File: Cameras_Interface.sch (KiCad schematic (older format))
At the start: 18 parts

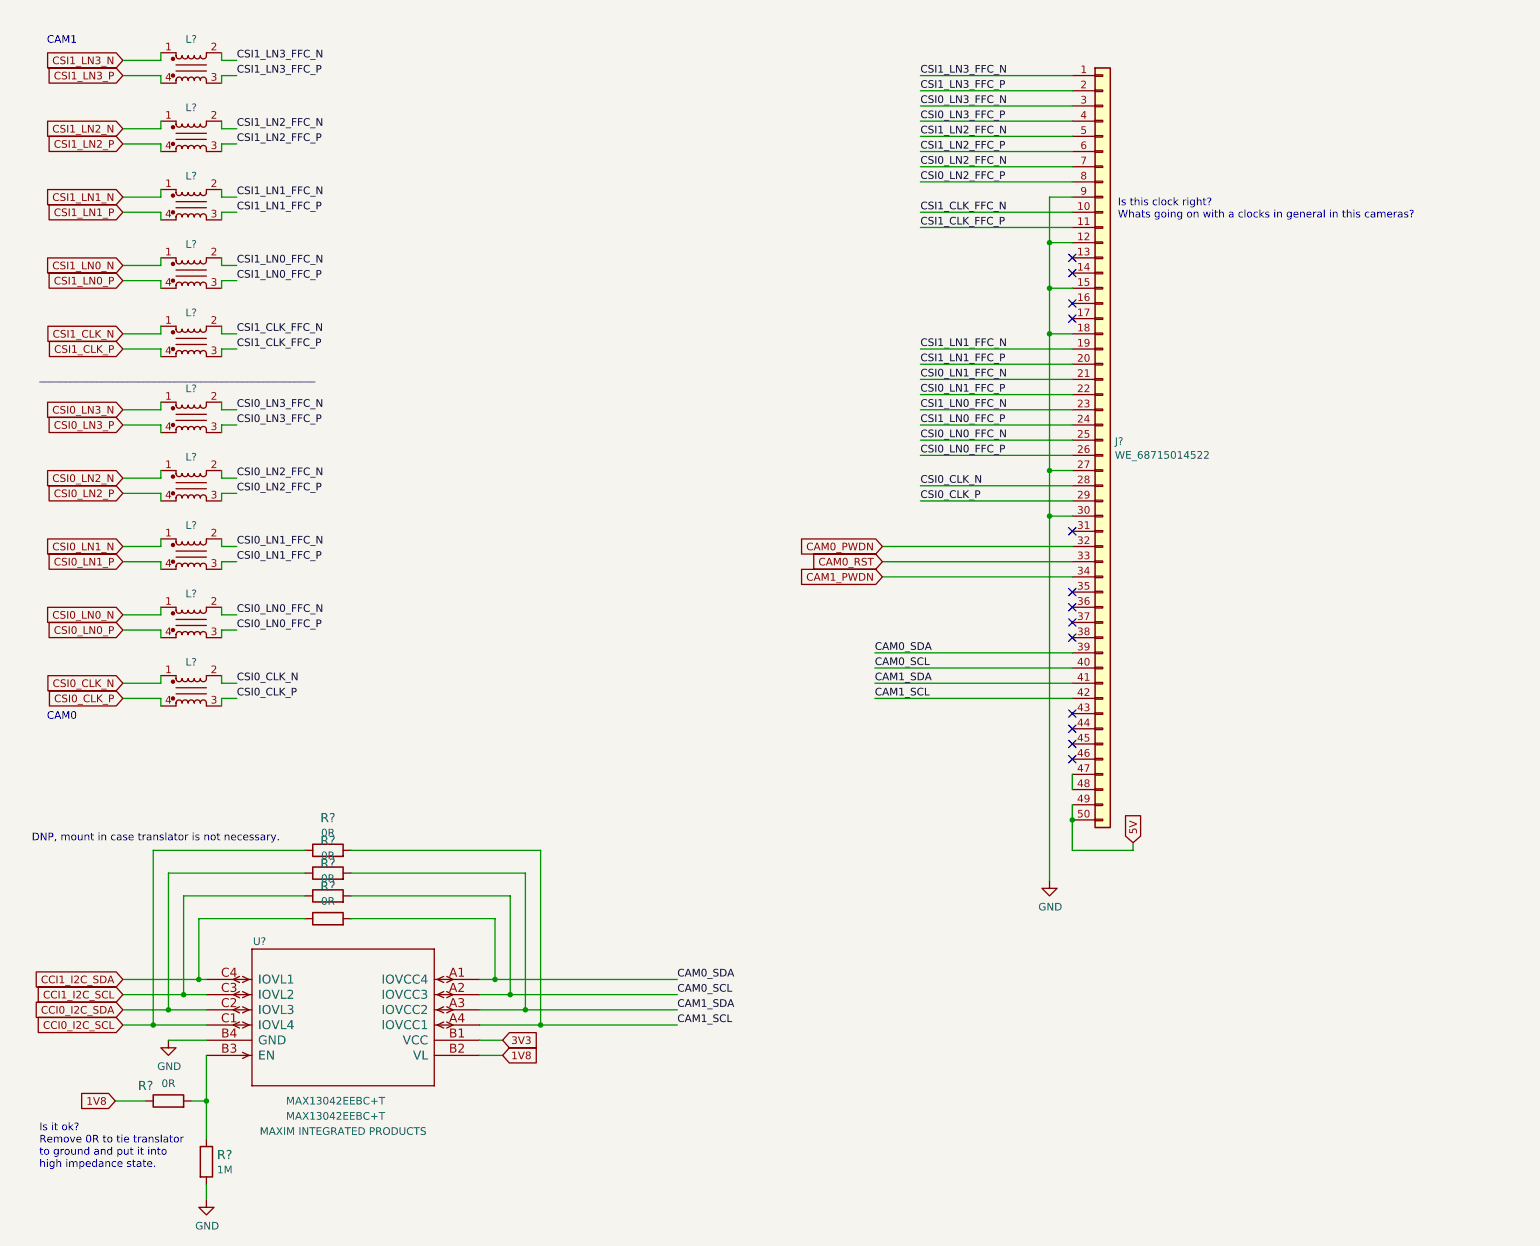
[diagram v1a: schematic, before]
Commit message: added components to pcb and fixed corresponding errors
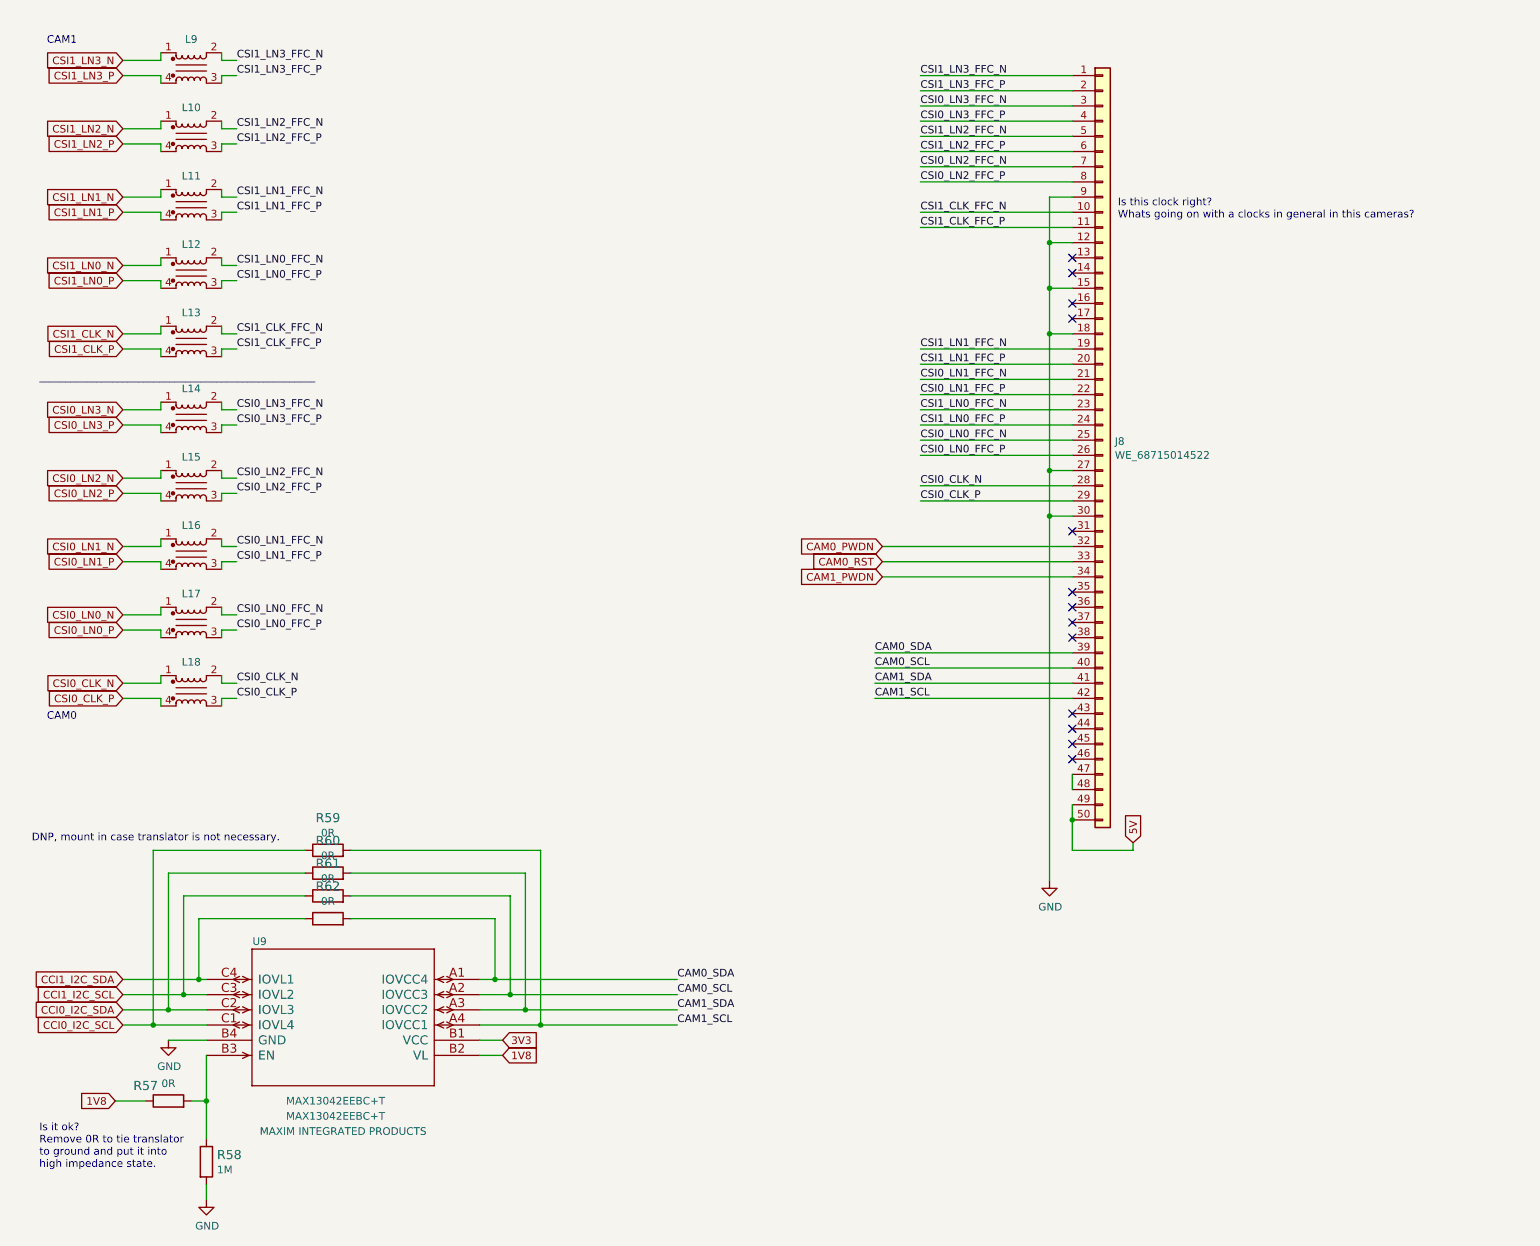
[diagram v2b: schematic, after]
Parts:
- gave numbers to parts that had none: 18
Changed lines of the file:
@@
 $Descr A3 16535 11693
 encoding utf-8
-Sheet 9 10
+Sheet 8 10
 Title ""
 Date ""
@@
 $EndDescr
 $Comp
-L antmicroFixedInductors:744235900 L?
+L antmicroFixedInductors:744235900 L14
 U 1 1 61A76D63
 P 1650 3900
-F 0 "L?" H 1650 4089 50  0000 C CNN
+F 0 "L14" H 1650 4089 50  0000 C CNN
 F 1 "744235900" H 1650 3725 50  0001 C CNN
 F 2 "antmicro-footprints:744235900" H 2250 4400 50  0001 C CNN
@@
 	1450 4700 1450 4750
 $Comp
-L antmicroFixedInductors:744235900 L?
+L antmicroFixedInductors:744235900 L16
 U 1 1 61AA8ED1
 P 1650 4800
-F 0 "L?" H 1650 4989 50  0000 C CNN
+F 0 "L16" H 1650 4989 50  0000 C CNN
 F 1 "744235900" H 1650 4625 50  0001 C CNN
 F 2 "antmicro-footprints:744235900" H 2250 5300 50  0001 C CNN
@@
 CSI0_LN1_N
 $Comp
-L antmicroFixedInductors:744235900 L?
+L antmicroFixedInductors:744235900 L15
 U 1 1 61AA3E09
 P 1650 4350
-F 0 "L?" H 1650 4539 50  0000 C CNN
+F 0 "L15" H 1650 4539 50  0000 C CNN
 F 1 "744235900" H 1650 4175 50  0001 C CNN
 F 2 "antmicro-footprints:744235900" H 2250 4850 50  0001 C CNN
@@
 CSI0_LN0_P
 $Comp
-L antmicroFixedInductors:744235900 L?
+L antmicroFixedInductors:744235900 L17
 U 1 1 61AB8175
 P 1650 5250
-F 0 "L?" H 1650 5439 50  0000 C CNN
+F 0 "L17" H 1650 5439 50  0000 C CNN
 F 1 "744235900" H 1650 5075 50  0001 C CNN
 F 2 "antmicro-footprints:744235900" H 2250 5750 50  0001 C CNN
@@
 CSI0_CLK_P
 $Comp
-L antmicroFixedInductors:744235900 L?
+L antmicroFixedInductors:744235900 L18
 U 1 1 61AD6420
 P 1650 5700
-F 0 "L?" H 1650 5889 50  0000 C CNN
+F 0 "L18" H 1650 5889 50  0000 C CNN
 F 1 "744235900" H 1650 5525 50  0001 C CNN
 F 2 "antmicro-footprints:744235900" H 2250 6200 50  0001 C CNN
@@
 	1450 5750 1200 5750
 $Comp
-L antmicroFixedInductors:744235900 L?
+L antmicroFixedInductors:744235900 L9
 U 1 1 61AE220C
 P 1650 1600
-F 0 "L?" H 1650 1789 50  0000 C CNN
+F 0 "L9" H 1650 1789 50  0000 C CNN
 F 1 "744235900" H 1650 1425 50  0001 C CNN
 F 2 "antmicro-footprints:744235900" H 2250 2100 50  0001 C CNN
@@
 	1450 2400 1450 2450
 $Comp
-L antmicroFixedInductors:744235900 L?
+L antmicroFixedInductors:744235900 L11
 U 1 1 61AE2229
 P 1650 2500
-F 0 "L?" H 1650 2689 50  0000 C CNN
+F 0 "L11" H 1650 2689 50  0000 C CNN
 F 1 "744235900" H 1650 2325 50  0001 C CNN
 F 2 "antmicro-footprints:744235900" H 2250 3000 50  0001 C CNN
@@
 CSI1_LN1_N
 $Comp
-L antmicroFixedInductors:744235900 L?
+L antmicroFixedInductors:744235900 L10
 U 1 1 61AE2236
 P 1650 2050
-F 0 "L?" H 1650 2239 50  0000 C CNN
+F 0 "L10" H 1650 2239 50  0000 C CNN
 F 1 "744235900" H 1650 1875 50  0001 C CNN
 F 2 "antmicro-footprints:744235900" H 2250 2550 50  0001 C CNN
@@
 CSI1_LN0_P
 $Comp
-L antmicroFixedInductors:744235900 L?
+L antmicroFixedInductors:744235900 L12
 U 1 1 61AE2243
 P 1650 2950
-F 0 "L?" H 1650 3139 50  0000 C CNN
+F 0 "L12" H 1650 3139 50  0000 C CNN
 F 1 "744235900" H 1650 2775 50  0001 C CNN
 F 2 "antmicro-footprints:744235900" H 2250 3450 50  0001 C CNN
@@
 CSI1_CLK_P
 $Comp
-L antmicroFixedInductors:744235900 L?
+L antmicroFixedInductors:744235900 L13
 U 1 1 61AE2254
 P 1650 3400
-F 0 "L?" H 1650 3589 50  0000 C CNN
+F 0 "L13" H 1650 3589 50  0000 C CNN
 F 1 "744235900" H 1650 3225 50  0001 C CNN
 F 2 "antmicro-footprints:744235900" H 2250 3900 50  0001 C CNN
@@
 	1450 3450 1200 3450
 $Comp
-L antmicroFCCConnectors:WE_68715014522 J?
+L antmicroFCCConnectors:WE_68715014522 J8
 U 1 1 61A63D9B
 P 7650 3250
-F 0 "J?" H 7730 2442 50  0000 L CNN
+F 0 "J8" H 7730 2442 50  0000 L CNN
 F 1 "WE_68715014522" H 7730 2351 50  0000 L CNN
 F 2 "antmicro-footprints:WE_68715014522" H 7450 -300 50  0001 C CNN
@@
 CAM1\n
 $Comp
-L power:GND #PWR?
+L power:GND #PWR056
 U 1 1 61C4B844
 P 7300 6950
-F 0 "#PWR?" H 7300 6700 50  0001 C CNN
+F 0 "#PWR056" H 7300 6700 50  0001 C CNN
 F 1 "GND" H 7305 6777 50  0000 C CNN
 F 2 "" H 7300 6950 50  0001 C CNN
@@
 $EndComp
 $Comp
-L antmicroLogicTranslatorsLevelShifters:MAX13042EEBC+T U?
+L antmicroLogicTranslatorsLevelShifters:MAX13042EEBC+T U9
 U 1 1 61C766BC
 P 3250 7400
-F 0 "U?" H 4400 7450 50  0000 C CNN
+F 0 "U9" H 4400 7450 50  0000 C CNN
 F 1 "MAX13042EEBC+T" H 3900 6400 50  0000 C CNN
 F 2 "antmicro-footprints:max13042eebc&plus_t" H 3250 7400 50  0001 C CNN
@@
 	3550 8100 3700 8100
 $Comp
-L power:GND #PWR?
+L power:GND #PWR054
 U 1 1 61CBF74D
 P 1500 8000
-F 0 "#PWR?" H 1500 7750 50  0001 C CNN
+F 0 "#PWR054" H 1500 7750 50  0001 C CNN
 F 1 "GND" H 1505 7827 50  0000 C CNN
 F 2 "" H 1500 8000 50  0001 C CNN
@@
 1V8
 $Comp
-L antmicroResistors0603:R_0R_0603 R?
+L antmicroResistors0603:R_0R_0603 R59
 U 1 1 61CF2C26
 P 2550 6750
-F 0 "R?" H 2550 6963 60  0000 C CNN
+F 0 "R59" H 2550 6963 60  0000 C CNN
 F 1 "R_0R_0603" H 2550 6600 60  0001 C CNN
 F 2 "antmicro-footprints:0603-res" H 2750 6950 60  0001 L CNN
@@
 $EndComp
 $Comp
-L antmicroResistors0603:R_0R_0603 R?
+L antmicroResistors0603:R_0R_0603 R60
 U 1 1 61CF310B
 P 2550 6900
-F 0 "R?" H 2550 7113 60  0000 C CNN
+F 0 "R60" H 2550 7113 60  0000 C CNN
 F 1 "R_0R_0603" H 2550 6750 60  0001 C CNN
 F 2 "antmicro-footprints:0603-res" H 2750 7100 60  0001 L CNN
@@
 $EndComp
 $Comp
-L antmicroResistors0603:R_0R_0603 R?
+L antmicroResistors0603:R_0R_0603 R61
 U 1 1 61CF351C
 P 2550 7050
-F 0 "R?" H 2550 7263 60  0000 C CNN
+F 0 "R61" H 2550 7263 60  0000 C CNN
 F 1 "R_0R_0603" H 2550 6900 60  0001 C CNN
 F 2 "antmicro-footprints:0603-res" H 2750 7250 60  0001 L CNN
@@
 $EndComp
 $Comp
-L antmicroResistors0603:R_0R_0603 R?
+L antmicroResistors0603:R_0R_0603 R62
 U 1 1 61CF37C7
 P 2550 7200
-F 0 "R?" H 2550 7413 60  0000 C CNN
+F 0 "R62" H 2550 7413 60  0000 C CNN
 F 1 "R_0R_0603" H 2550 7050 60  0001 C CNN
 F 2 "antmicro-footprints:0603-res" H 2750 7400 60  0001 L CNN
@@
 	3950 7900 4850 7900
 $Comp
-L power:GND #PWR?
+L power:GND #PWR055
 U 1 1 61D3BC05
 P 1750 9050
-F 0 "#PWR?" H 1750 8800 50  0001 C CNN
+F 0 "#PWR055" H 1750 8800 50  0001 C CNN
 F 1 "GND" H 1755 8877 50  0000 C CNN
 F 2 "" H 1750 9050 50  0001 C CNN
@@
 $EndComp
 $Comp
-L antmicroResistors0603:R_1M_0603 R?
+L antmicroResistors0603:R_1M_0603 R58
 U 1 1 61D3BF41
 P 1750 8800
-F 0 "R?" V 1705 8870 60  0000 L CNN
+F 0 "R58" V 1705 8870 60  0000 L CNN
 F 1 "R_1M_0603" H 1750 8650 60  0001 C CNN
 F 2 "antmicro-footprints:0603-res" H 1950 9000 60  0001 L CNN
@@
 	1150 8400 1350 8400
 $Comp
-L antmicroResistors0603:R_0R_0603 R?
+L antmicroResistors0603:R_0R_0603 R57
 U 1 1 61D62802
 P 1500 8400
-F 0 "R?" H 1350 8500 60  0000 C CNN
+F 0 "R57" H 1350 8500 60  0000 C CNN
 F 1 "R_0R_0603" H 1500 8250 60  0001 C CNN
 F 2 "antmicro-footprints:0603-res" H 1700 8600 60  0001 L CNN

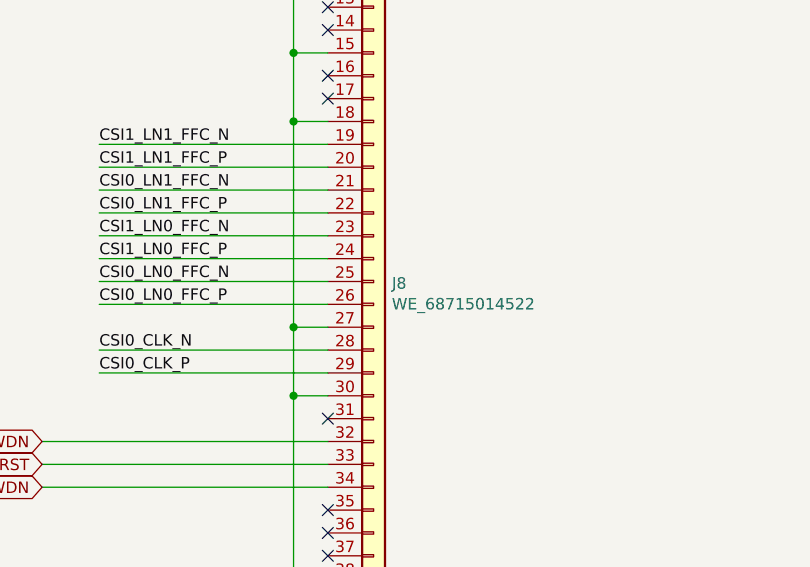
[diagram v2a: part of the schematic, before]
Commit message: added first version of board layout
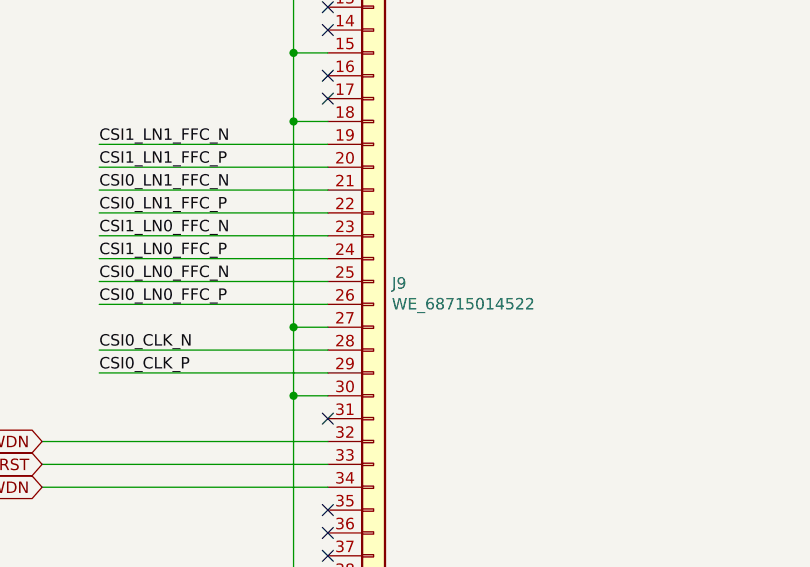
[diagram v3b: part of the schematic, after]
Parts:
- renumbered J8 to J9
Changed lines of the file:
@@
 $Descr A3 16535 11693
 encoding utf-8
-Sheet 8 10
+Sheet 8 11
 Title ""
 Date ""
@@
 	1450 3450 1200 3450
 $Comp
-L antmicroFCCConnectors:WE_68715014522 J8
+L antmicroFCCConnectors:WE_68715014522 J9
 U 1 1 61A63D9B
 P 7650 3250
-F 0 "J8" H 7730 2442 50  0000 L CNN
+F 0 "J9" H 7730 2442 50  0000 L CNN
 F 1 "WE_68715014522" H 7730 2351 50  0000 L CNN
 F 2 "antmicro-footprints:WE_68715014522" H 7450 -300 50  0001 C CNN
@@
 CAM1\n
 $Comp
-L power:GND #PWR056
+L power:GND #PWR066
 U 1 1 61C4B844
 P 7300 6950
-F 0 "#PWR056" H 7300 6700 50  0001 C CNN
+F 0 "#PWR066" H 7300 6700 50  0001 C CNN
 F 1 "GND" H 7305 6777 50  0000 C CNN
 F 2 "" H 7300 6950 50  0001 C CNN
@@
 	3550 8100 3700 8100
 $Comp
-L power:GND #PWR054
+L power:GND #PWR064
 U 1 1 61CBF74D
 P 1500 8000
-F 0 "#PWR054" H 1500 7750 50  0001 C CNN
+F 0 "#PWR064" H 1500 7750 50  0001 C CNN
 F 1 "GND" H 1505 7827 50  0000 C CNN
 F 2 "" H 1500 8000 50  0001 C CNN
@@
 	3950 7900 4850 7900
 $Comp
-L power:GND #PWR055
+L power:GND #PWR065
 U 1 1 61D3BC05
 P 1750 9050
-F 0 "#PWR055" H 1750 8800 50  0001 C CNN
+F 0 "#PWR065" H 1750 8800 50  0001 C CNN
 F 1 "GND" H 1755 8877 50  0000 C CNN
 F 2 "" H 1750 9050 50  0001 C CNN
